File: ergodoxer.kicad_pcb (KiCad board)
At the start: 2 copper layers, 313.8 x 174.1 mm, 155 parts, among them J1 USB_C_Receptacle, SW1 SW_Push_mod, SW10 SW_Push, SW11 SW_Push, SW12 SW_Push, SW13 SW_Push_mod, SW14 SW_Push, SW15 SW_Push, SW16 SW_Push, SW17 SW_Push, SW18 SW_Push, SW19 SW_Push_mod, SW2 SW_Push, SW20 SW_Push, SW21 SW_Push, SW22 SW_Push, SW23 SW_Push, SW24 SW_Push, SW25 SW_Push_mod, SW26 SW_Push, SW27 SW_Push, SW28 SW_Push, SW29 SW_Push, SW3 SW_Push, SW30 SW_Push, SW31 SW_Push_mod, SW32 SW_Push, SW33 SW_Push, SW34 SW_Push, SW35 SW_Push, SW37 SW_Push_mod, SW38 SW_Push, SW39 SW_Push, SW4 SW_Push, SW40 SW_Push, SW41 SW_Push, SW43 SW_Push, SW44 SW_Push, SW45 SW_Push, SW46 SW_Push, SW47 SW_Push, SW48 SW_Push, SW49 SW_Push, SW5 SW_Push, SW50 SW_Push, SW51 SW_Push, SW52 SW_Push, SW53 SW_Push, SW6 SW_Push, SW7 SW_Push_mod, SW8 SW_Push, SW9 SW_Push, U1 Proton_C

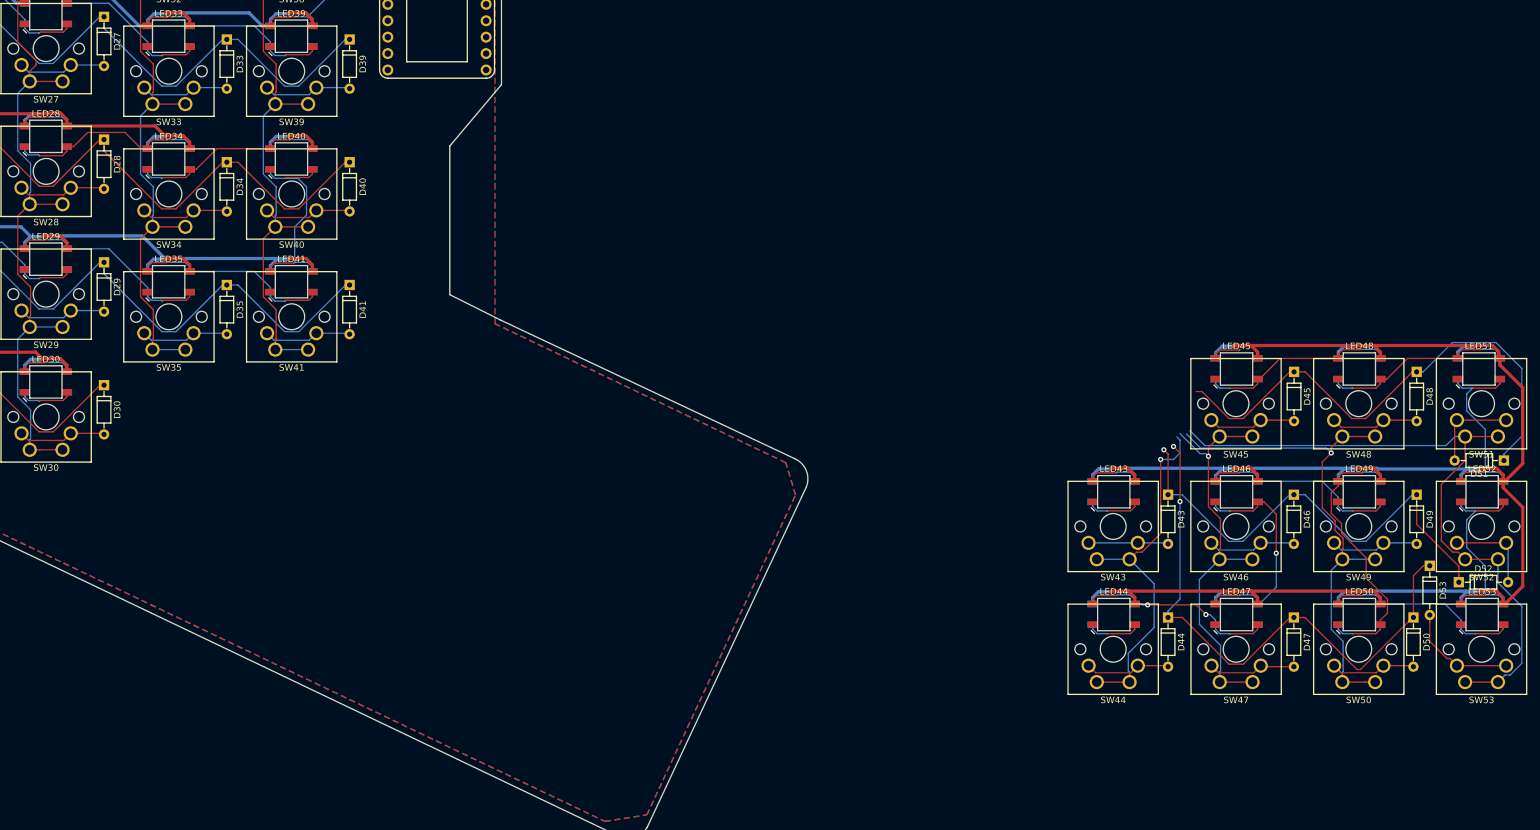
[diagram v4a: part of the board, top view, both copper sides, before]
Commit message: Add qmk hardware as a submodule and connect thumb cluster
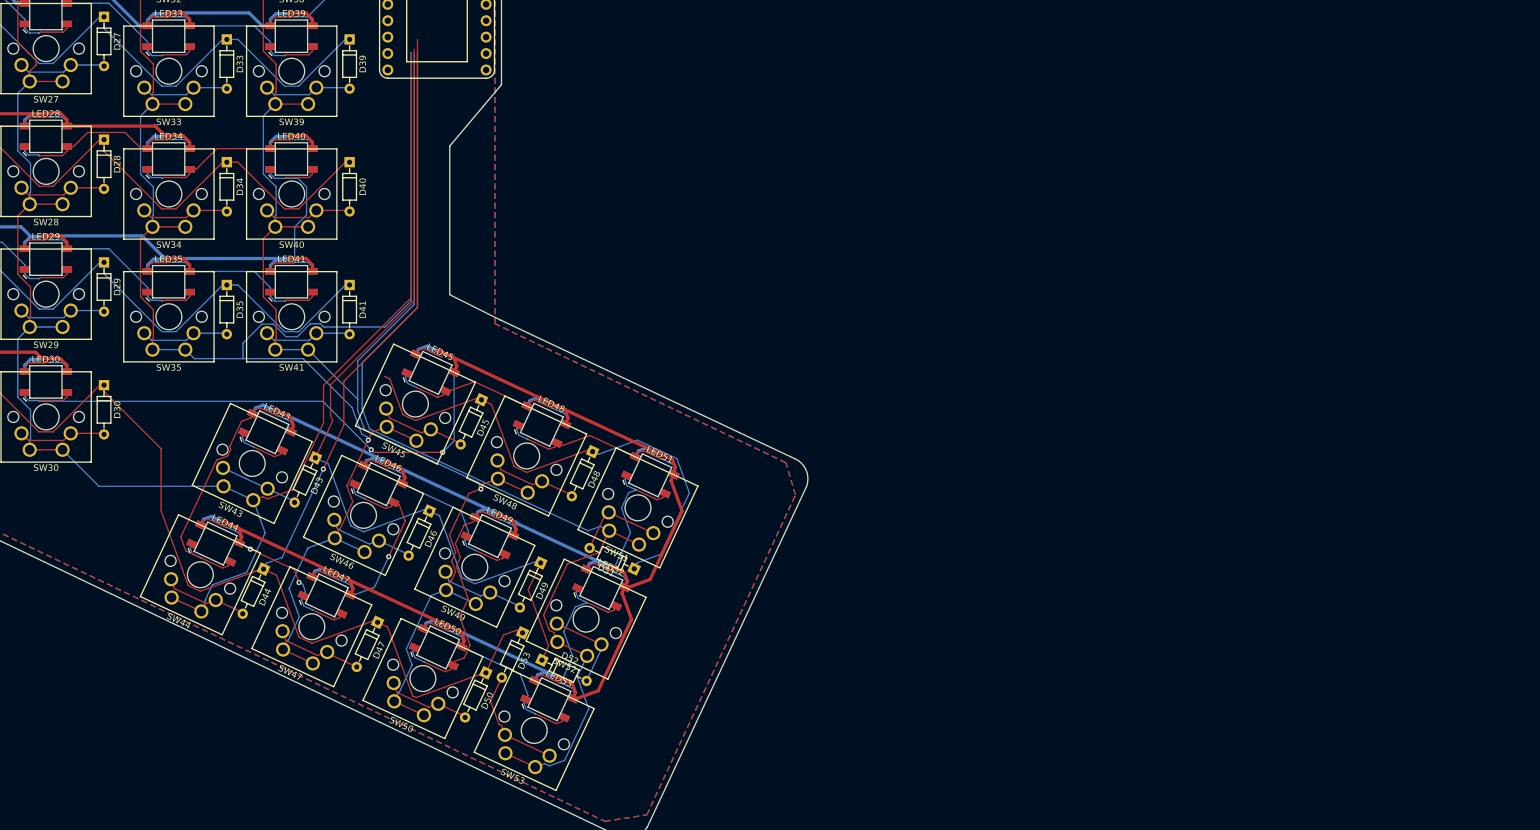
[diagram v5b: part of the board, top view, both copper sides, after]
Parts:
- U1: value Proton_C -> proton_c
- moved SW53 148.9 mm to (223.6, 180.5), turned to 155 degrees
- moved SW50 146.8 mm to (206.4, 172.4), turned to 155 degrees
- moved SW47 145.0 mm to (189.2, 164.4), turned to 155 degrees
- moved LED53 144.9 mm to (230.4, 172.1), turned to 335 degrees
- moved D50 143.8 mm to (220.6, 168.0), turned to 245 degrees
- moved SW44 143.8 mm to (172.0, 156.4), turned to 155 degrees
- moved LED50 142.6 mm to (213.2, 164.0), turned to 335 degrees
- moved D52 142.4 mm to (229.3, 166.0), turned to 335 degrees
- moved D47 141.8 mm to (203.8, 160.2), turned to 245 degrees
- moved SW52 141.1 mm to (231.6, 163.2), turned to 155 degrees
- moved LED47 140.8 mm to (196.0, 156.0), turned to 335 degrees
- moved D53 140.8 mm to (226.3, 161.8), turned to 245 degrees
- moved D44 140.2 mm to (186.2, 152.0), turned to 245 degrees
- moved LED44 139.4 mm to (178.8, 148.0), turned to 335 degrees
- moved SW49 138.8 mm to (214.4, 155.2), turned to 155 degrees
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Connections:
- D43 pad 1: row7 -> row8
- D44 pad 1: row8 -> row6
- D45 pad 1: row6 -> row7
- D46 pad 1: row7 -> row8
- D47 pad 1: row8 -> row6
- D48 pad 1: row6 -> row7
- D49 pad 1: row7 -> row8
- D50 pad 1: row8 -> row6
- D51 pad 1: row6 -> row7
- D52 pad 1: row7 -> row8
- D53 pad 1: row8 -> row6
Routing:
- net row6: track 177.9 -> 297.2 mm, vias 0 -> 1
- net column6: track 215.1 -> 316.2 mm
- net column5: track 254.9 -> 338.4 mm, vias 2 -> 1
- net Net-(LED30-Pad2): track 13.2 -> 92.0 mm, vias 0 -> 2
- net column7: track 215.9 -> 285.9 mm
- net column8: track 104.5 -> 163.2 mm
- net row8: track 87.9 -> 135.9 mm, vias 2 -> 0
- net Net-(LED43-Pad4): track 17.0 -> 45.1 mm
- net row7: track 73.9 -> 79.4 mm, vias 1 -> 0
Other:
- board size 313.8 x 174.1 mm -> 207 x 174.1 mm

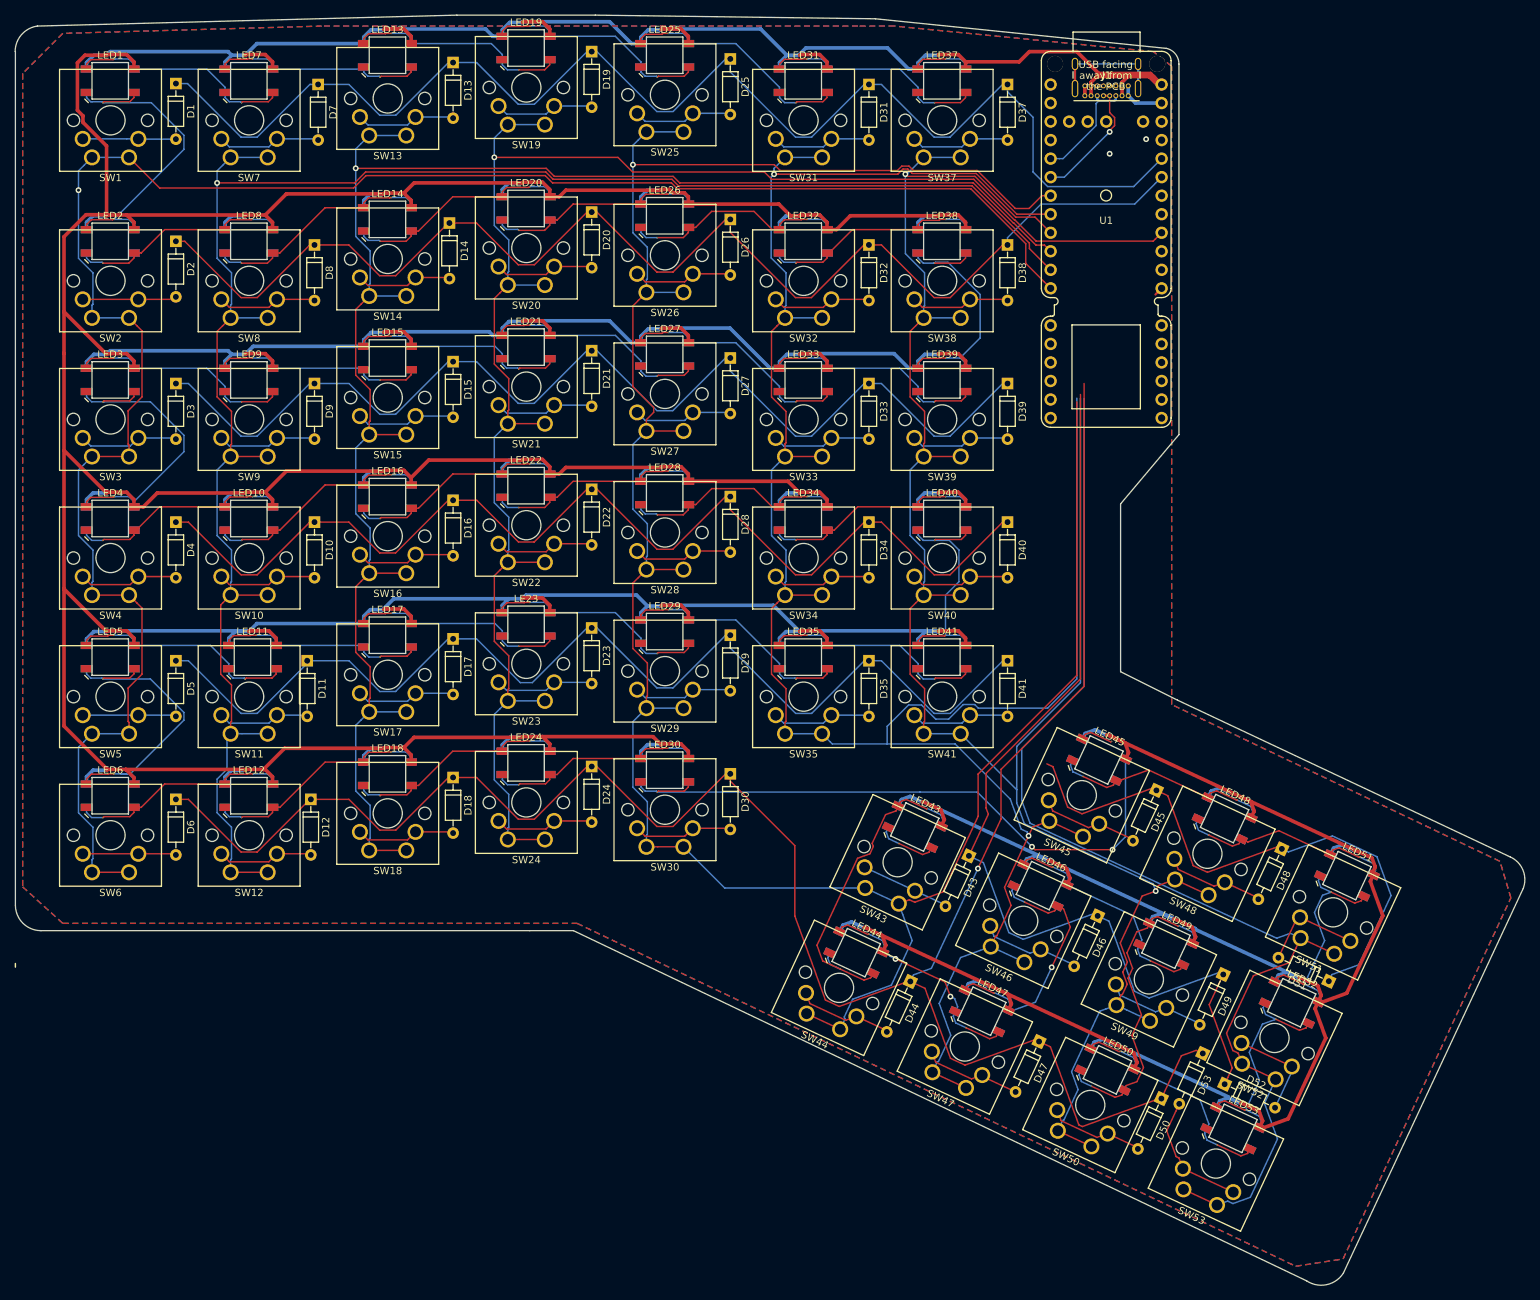
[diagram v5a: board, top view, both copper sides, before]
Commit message: Redo thumb cluster
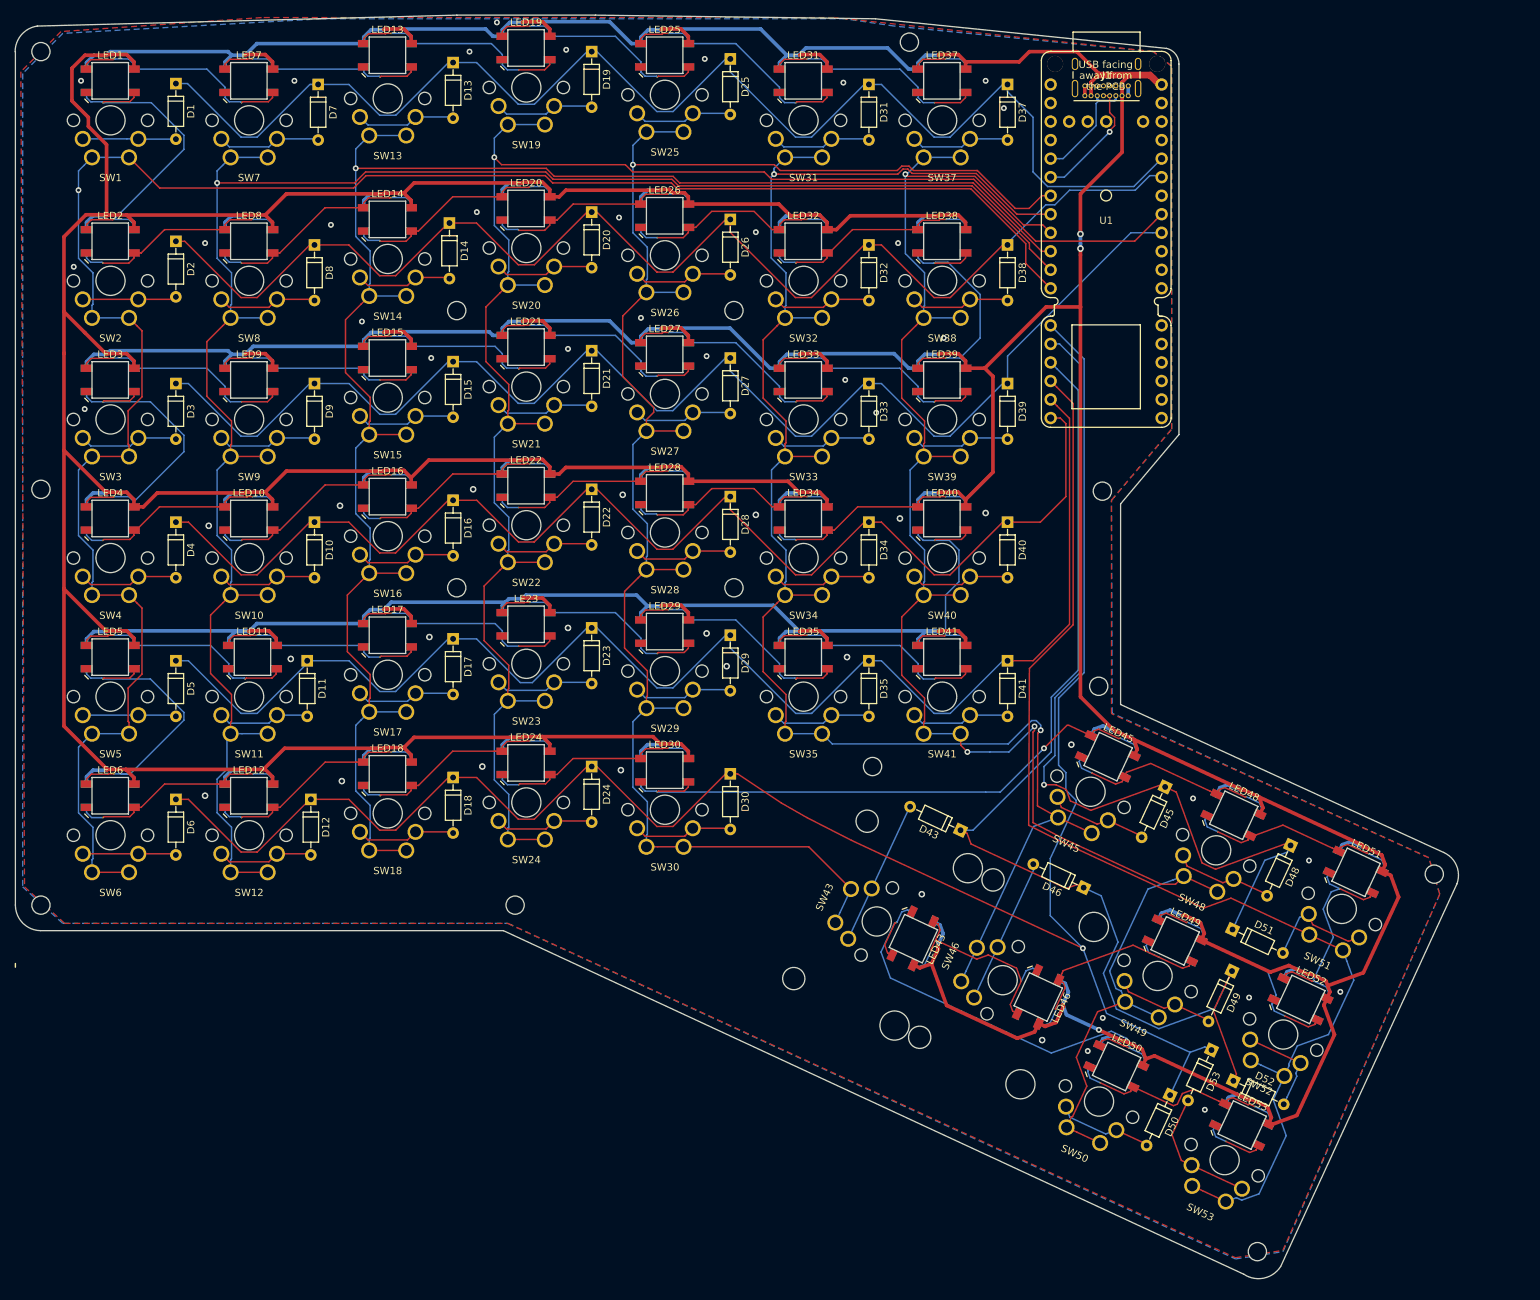
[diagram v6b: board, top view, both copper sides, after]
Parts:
- removed D44, D47: 1N4148, Diodes_ThroughHole:D_DO-35_SOD27_P7.62mm_Horizontal
- removed LED44: WS2812, switches:LED_WS2812B-inverted
- removed LED47: WS2812B, switches:LED_WS2812B-inverted
- removed SW44, SW47: SW_Push, switches:SW_Cherry_MX_1.00u_PCB_dual
- added REF**: MountingHole_2.5mm, Mounting_Holes:MountingHole_2.5mm, F.Cu at (124.0, 98.0)
- added REF**: MountingHole_2.5mm, Mounting_Holes:MountingHole_2.5mm, F.Cu at (186.1, 23.2)
- added REF**: MountingHole_2.5mm, Mounting_Holes:MountingHole_2.5mm, F.Cu at (212.5, 84.8)
- added REF**: MountingHole_2.5mm, Mounting_Holes:MountingHole_2.5mm, F.Cu at (212.0, 111.5)
- added REF**: MountingHole_2.5mm, Mounting_Holes:MountingHole_2.5mm, F.Cu at (258.0, 137.2)
- added REF**: MountingHole_2.5mm, Mounting_Holes:MountingHole_2.5mm, F.Cu at (233.8, 189.0)
- added REF**: MountingHole_2.5mm, Mounting_Holes:MountingHole_2.5mm, F.Cu at (124.0, 60.0)
- added REF**: MountingHole_2.5mm, Mounting_Holes:MountingHole_2.5mm, F.Cu at (162.0, 60.0)
- added REF**: MountingHole_2.5mm, Mounting_Holes:MountingHole_2.5mm, F.Cu at (162.0, 98.0)
- added REF**: MountingHole_2.5mm, Mounting_Holes:MountingHole_2.5mm, F.Cu at (181.0, 122.5)
- added REF**: MountingHole_2.5mm, Mounting_Holes:MountingHole_2.5mm, F.Cu at (132.0, 141.5)
- added REF**: MountingHole_2.5mm, Mounting_Holes:MountingHole_2.5mm, F.Cu at (67.0, 141.5)
- added REF**: MountingHole_2.5mm, Mounting_Holes:MountingHole_2.5mm, F.Cu at (67.0, 84.5)
- added REF**: MountingHole_2.5mm, Mounting_Holes:MountingHole_2.5mm, F.Cu at (67.0, 24.5)
- SW43, SW46: footprint switches:SW_Cherry_MX_1.00u_PCB_dual -> switches:SW_Cherry_MX_2.00u_PCB_reversible
- moved LED43 15.3 mm to (186.5, 146.1), turned to 245 degrees
- moved LED46 15.3 mm to (203.7, 154.1), turned to 245 degrees
- moved D51 15.0 mm to (230.3, 144.8), turned to 335 degrees
- moved D46 4.32 mm to (209.9, 139.1), turned to 155 degrees
- moved D43 3.70 mm to (193.1, 131.2), turned to 155 degrees
- moved SW43 1.95 mm to (178.0, 139.3), turned to 65 degrees
- moved SW46 1.91 mm to (195.3, 147.3), turned to 65 degrees
- moved LED52 1.29 mm to (239.7, 154.4)
- moved LED49 1.29 mm to (222.4, 146.3)
- moved D48 1.29 mm to (238.3, 133.3)
- moved D52 1.29 mm to (230.5, 165.6)
- moved LED48 1.29 mm to (230.5, 129.1)
- moved D45 1.29 mm to (221.1, 125.3)
- moved D49 1.29 mm to (230.3, 150.5)
- moved D53 1.29 mm to (227.5, 161.4)
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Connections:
- J1 pad S1: Net-(J1-PadS1) -> GND
- LED46 pad 2: Net-(LED46-Pad2) -> Net-(LED43-Pad4)
- LED50 pad 2: Net-(LED49-Pad4) -> Net-(LED50-Pad2)
- LED50 pad 4: Net-(LED50-Pad4) -> Net-(LED43-Pad2)
- LED52 pad 2: Net-(LED52-Pad2) -> Net-(LED49-Pad4)
- LED53 pad 2: Net-(LED50-Pad4) -> Net-(LED53-Pad2)
- LED53 pad 4: Net-(LED52-Pad2) -> Net-(LED50-Pad2)
- U1 pad A0: row3 -> Net-(U1-PadA0)
- U1 pad A15: Net-(U1-PadA15) -> row4
- U1 pad A4: row5 -> row6
- U1 pad A5: row6 -> row7
- U1 pad A6: Net-(U1-PadA6) -> row8
- U1 pad A7: Net-(U1-PadA7) -> column8
- U1 pad A8: Net-(U1-PadA8) -> row5
- U1 pad B10: column8 -> Net-(U1-PadB10)
- U1 pad B11: row8 -> Net-(U1-PadB11)
- U1 pad B12: row7 -> Net-(U1-PadB12)
- U1 pad B13: column4 -> row3
- U1 pad B8: row4 -> column4
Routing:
- net column5: track 338.4 -> 230.9 mm
- net column6: track 316.2 -> 232.4 mm
- net VBUS: track 1407.9 -> 1472.6 mm, vias 0 -> 3
- net Net-(LED43-Pad2): track 8.50 -> 62.3 mm
- net row7: track 79.4 -> 123.9 mm, vias 0 -> 1
- net row5: track 151.4 -> 193.8 mm
- net column7: track 285.9 -> 245.8 mm, vias 2 -> 3
- net Net-(LED46-Pad2): track 36.0 -> 0.00 mm, vias 1 -> 0
- net row3: track 150.9 -> 182.8 mm
- net Net-(LED50-Pad2): track 0.00 -> 31.8 mm
- net Net-(LED52-Pad2): track 31.8 -> 0.00 mm
- net Net-(LED44-Pad4): track 31.2 -> 0.00 mm, vias 2 -> 0
- net Net-(LED50-Pad4): track 31.2 -> 0.00 mm
- net row4: track 150.9 -> 172.8 mm
- net row6: track 297.2 -> 276.7 mm
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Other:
- board size 207 x 174.1 mm -> 197.9 x 173.2 mm
- net class power: via_dia 0.8 -> 0.9; via_drill 0.4 -> 0.5
